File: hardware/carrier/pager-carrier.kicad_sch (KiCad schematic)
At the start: 0 parts

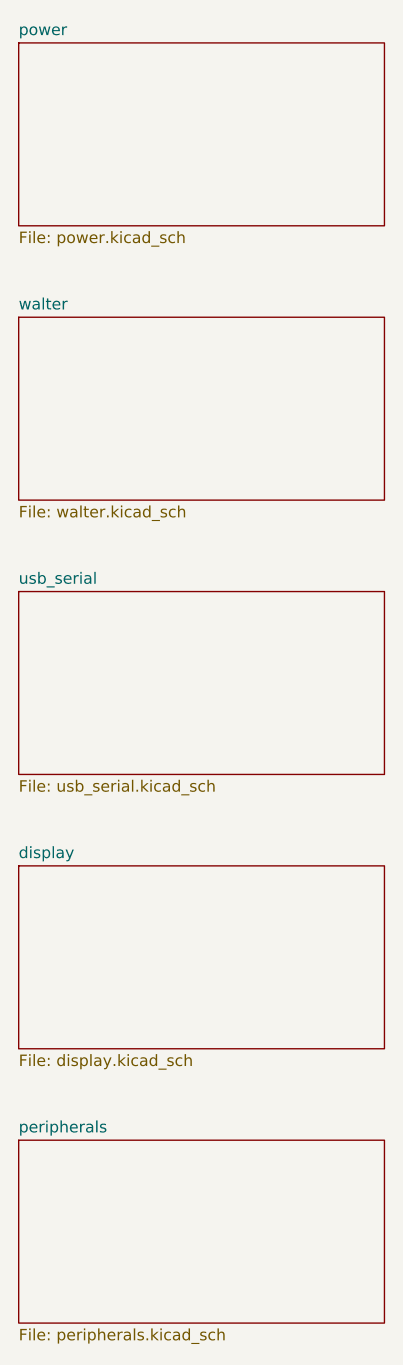
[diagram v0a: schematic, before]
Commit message: Manually review and fix carrier board schematic
The initial product of clause was mostly okay electrically
but impossible to read. This is a fully redone version
that has all circuits reverified with some modifications.
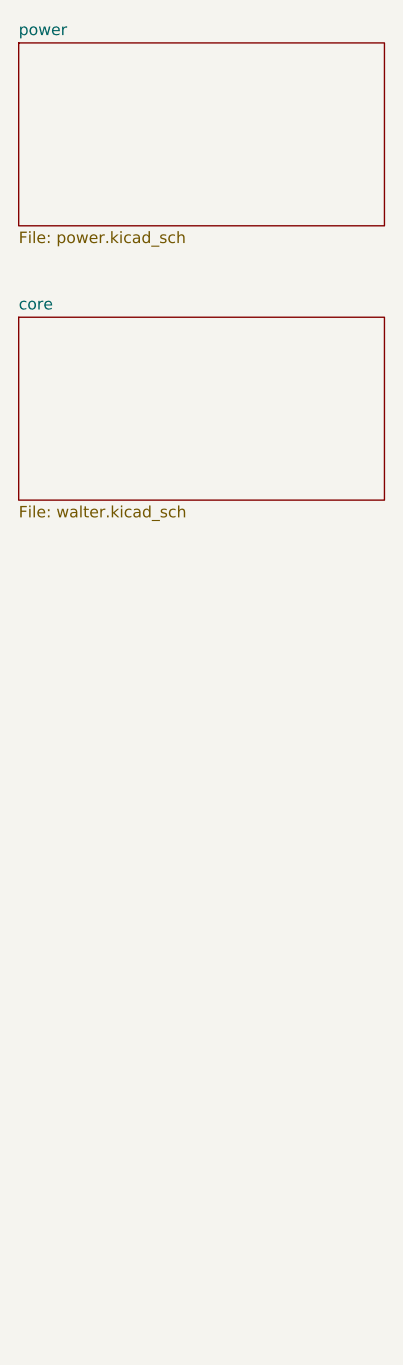
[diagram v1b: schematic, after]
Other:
- sheet walter renamed core
- removed sheet display
- removed sheet peripherals
- removed sheet usb_serial
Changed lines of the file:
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@@
 		(property "Sheetname" "power"
 			(at 25.4 24.6884 0)
+			(show_name no)
+			(do_not_autoplace no)
 			(effects
 				(font
@@
 		(property "Sheetfile" "power.kicad_sch"
 			(at 25.4 46.3046 0)
+			(show_name no)
+			(do_not_autoplace no)
 			(effects
 				(font
@@
 			(color 0 0 0 0)
 		)
-		(property "Sheetname" "walter"
+		(property "Sheetname" "core"
 			(at 25.4 55.1684 0)
+			(show_name no)
+			(do_not_autoplace no)
 			(effects
 				(font
@@
 		(property "Sheetfile" "walter.kicad_sch"
 			(at 25.4 76.7846 0)
+			(show_name no)
+			(do_not_autoplace no)
 			(effects
 				(font
@@
 				)
 			)
-		)
-	)
-	(sheet
-		(at 25.4 86.36)
-		(size 40.64 20.32)
-		(exclude_from_sim no)
-		(in_bom yes)
-		(on_board yes)
-		(dnp no)
-		(fields_autoplaced yes)
-		(stroke
-			(width 0.1524)
-			(type solid)
-		)
-		(fill
-			(color 0 0 0 0)
-		)
-		(property "Sheetname" "usb_serial"
-			(at 25.4 85.6484 0)
-			(effects
-				(font
-					(size 1.27 1.27)
-				)
-				(justify left bottom)
-			)
-		)
-		(property "Sheetfile" "usb_serial.kicad_sch"
-			(at 25.4 107.2646 0)
-			(effects
-				(font
-					(size 1.27 1.27)
-				)
-				(justify left top)
-			)
-		)
-		(instances
-			(project "pager-carrier"
-				(path "/10ec5e8c-30f8-50c5-8dd4-a077611d8ec6"
-					(page "4")
-				)
-			)
-		)
-	)
-	(sheet
-		(at 25.4 116.84)
-		(size 40.64 20.32)
-		(exclude_from_sim no)
-		(in_bom yes)
-		(on_board yes)
-		(dnp no)
-		(fields_autoplaced yes)
-		(stroke
-			(width 0.1524)
-			(type solid)
-		)
-		(fill
-			(color 0 0 0 0)
-		)
-		(property "Sheetname" "display"
-			(at 25.4 116.1284 0)
-			(effects
-				(font
-					(size 1.27 1.27)
-				)
-				(justify left bottom)
-			)
-		)
-		(property "Sheetfile" "display.kicad_sch"
-			(at 25.4 137.7446 0)
-			(effects
-				(font
-					(size 1.27 1.27)
-				)
-				(justify left top)
-			)
-		)
-		(instances
-			(project "pager-carrier"
-				(path "/10ec5e8c-30f8-50c5-8dd4-a077611d8ec6"
-					(page "5")
-				)
-			)
-		)
-	)
-	(sheet
-		(at 25.4 147.32)
-		(size 40.64 20.32)
-		(exclude_from_sim no)
-		(in_bom yes)
-		(on_board yes)
-		(dnp no)
-		(fields_autoplaced yes)
-		(stroke
-			(width 0.1524)
-			(type solid)
-		)
-		(fill
-			(color 0 0 0 0)
-		)
-		(property "Sheetname" "peripherals"
-			(at 25.4 146.6084 0)
-			(effects
-				(font
-					(size 1.27 1.27)
-				)
-				(justify left bottom)
-			)
-		)
-		(property "Sheetfile" "peripherals.kicad_sch"
-			(at 25.4 168.2246 0)
-			(effects
-				(font
-					(size 1.27 1.27)
-				)
-				(justify left top)
-			)
-		)
-		(instances
-			(project "pager-carrier"
-				(path "/10ec5e8c-30f8-50c5-8dd4-a077611d8ec6"
-					(page "6")
-				)
-			)
